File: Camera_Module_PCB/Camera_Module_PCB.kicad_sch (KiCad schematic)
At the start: 80 parts, among them J3 FFC2A32-24-T, SW2 SW_Push, SW3 SW_Push, U2 ESP32-S3R8, U4 MAX98357AETE_T, U5 AP3032KTR-G1, Y1 Q40,0-JXS10-8-10/10-FU-LF1

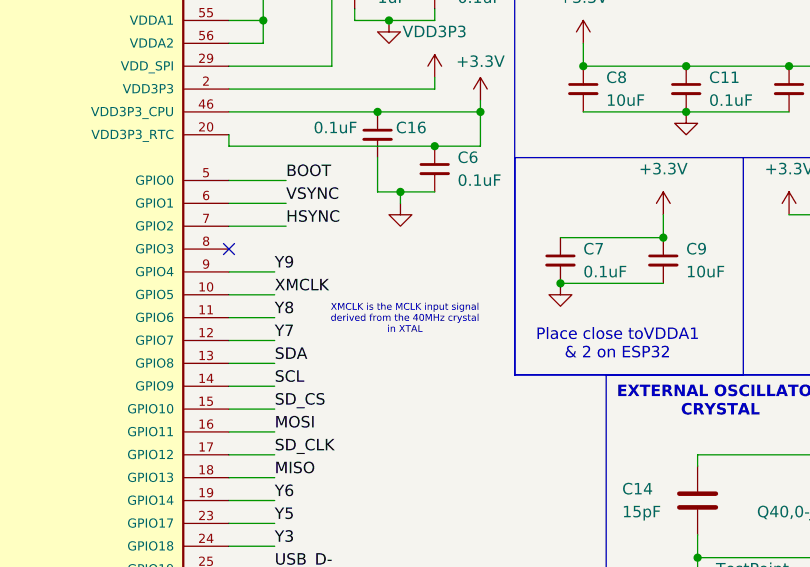
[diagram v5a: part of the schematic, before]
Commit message: Made some schematic edits & continued work on layout
Made some minor adjustments for the schematic to prepare for review. The layout continues to be built.
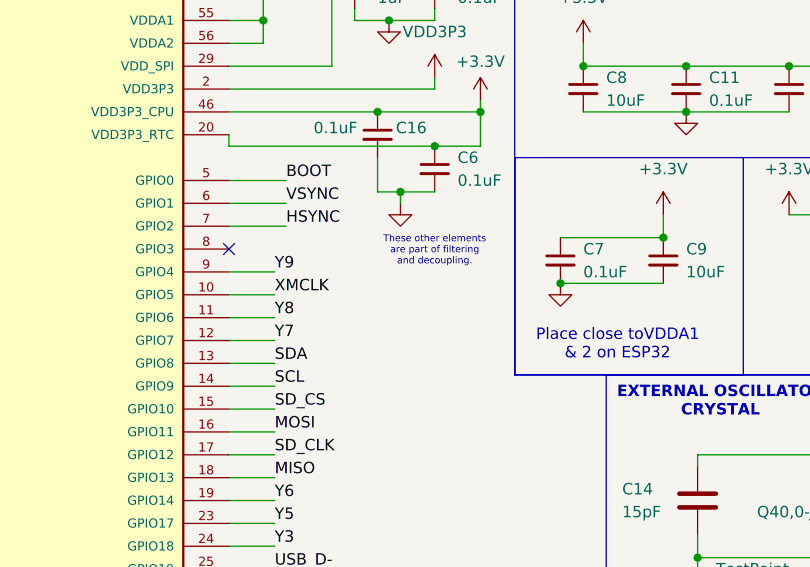
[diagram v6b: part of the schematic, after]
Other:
- note added: "These other elements are part of filtering and decoupling."
- note removed: "XMCLK is the MCLK input signal derived from the 40MHz crystal in XTAL"
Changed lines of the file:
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@@
 		(stroke
 			(width 0)
-			(type default)
+			(type solid)
+			(color 255 0 0 1)
 		)
 		(fill
@@
 		(stroke
 			(width 0)
-			(type default)
+			(type solid)
+			(color 250 0 0 1)
 		)
 		(fill
@@
 		(stroke
 			(width 0)
-			(type default)
+			(type solid)
+			(color 250 0 0 1)
 		)
 		(fill
@@
 		(stroke
 			(width 0)
-			(type default)
+			(type solid)
+			(color 251 0 0 1)
 		)
 		(fill
@@
 		)
 	)
-	(text "XMCLK is the MCLK input signal\nderived from the 40MHz crystal\nin XTAL"
+	(text "These other elements \nare part of filtering\nand decoupling.\n"
 		(exclude_from_sim no)
-		(at 320.548 59.944 0)
+		(at 323.85 52.324 0)
 		(effects
 			(font
 				(size 0.762 0.762)
+				(color 255 0 0 1)
 			)
 		)

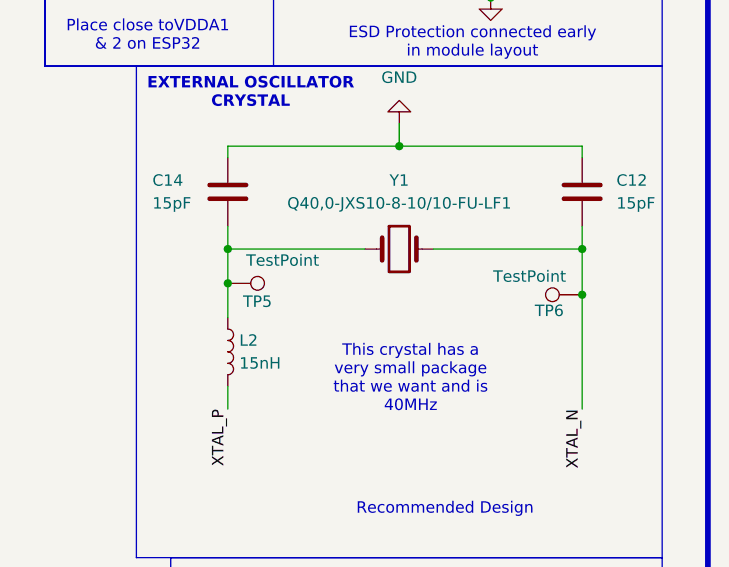
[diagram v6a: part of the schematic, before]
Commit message: Routed Antenna and Crystal
The antenna and crystals that connect to the ESP32-S3 were routed and a dense layer of ground vias were used for isolation along with no net filled zones. There is a small concern between the RF trace and the 3V3 analog power at pins 2 and 3. Due to DRC, I am unable to place vias between then. Perhaps much smaller vias can be used as a compromise.
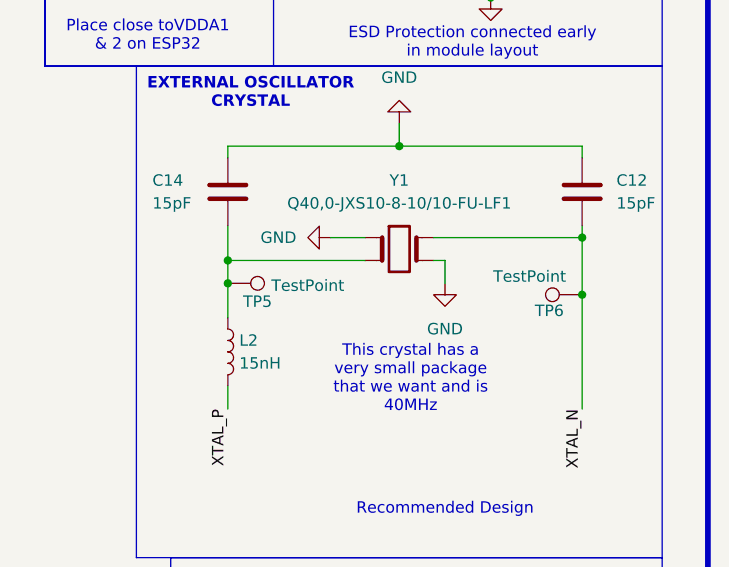
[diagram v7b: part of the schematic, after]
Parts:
- C7, C9: footprint Capacitor_SMD:C_0603_1608Metric -> Capacitor_SMD:C_0402_1005Metric
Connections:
- net GND: now also Y1.2 (Ground), Y1.4 (Ground)
- net XTAL_N: now also Y1.3 (Output); no longer Y1.2
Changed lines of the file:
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@@
 	)
 	(junction
+		(at 392.43 85.09)
+		(diameter 0)
+		(color 0 0 0 0)
+	)
+	(junction
 		(at 26.67 31.75)
 		(diameter 0)
@@
 	)
 	(junction
-		(at 392.43 86.36)
-		(diameter 0)
-		(color 0 0 0 0)
-	)
-	(junction
 		(at 114.3 45.72)
 		(diameter 0)
@@
 	)
 	(junction
+		(at 353.06 87.63)
+		(diameter 0)
+		(color 0 0 0 0)
+	)
+	(junction
 		(at 46.99 105.41)
 		(diameter 0)
@@
 	)
 	(junction
-		(at 353.06 86.36)
-		(diameter 0)
-		(color 0 0 0 0)
-	)
-	(junction
 		(at 198.12 74.93)
 		(diameter 0)
@@
 	(wire
 		(pts
-			(xy 353.06 86.36) (xy 353.06 90.17)
-		)
-		(stroke
-			(width 0)
-			(type default)
-		)
-	)
-	(wire
-		(pts
 			(xy 363.22 31.75) (xy 369.57 31.75)
 		)
@@
 	(wire
 		(pts
-			(xy 392.43 86.36) (xy 392.43 83.82)
-		)
-		(stroke
-			(width 0)
-			(type default)
-		)
-	)
-	(wire
-		(pts
 			(xy 20.32 105.41) (xy 21.59 105.41)
 		)
@@
 	(wire
 		(pts
-			(xy 353.06 83.82) (xy 353.06 86.36)
+			(xy 353.06 83.82) (xy 353.06 87.63)
 		)
 		(stroke
@@
 	(wire
 		(pts
+			(xy 377.19 87.63) (xy 377.19 90.17)
+		)
+		(stroke
+			(width 0)
+			(type default)
+		)
+	)
+	(wire
+		(pts
 			(xy 300.99 107.95) (xy 306.07 107.95)
 		)
@@
 	(wire
 		(pts
+			(xy 364.49 85.09) (xy 368.3 85.09)
+		)
+		(stroke
+			(width 0)
+			(type default)
+		)
+	)
+	(wire
+		(pts
 			(xy 382.27 137.16) (xy 382.27 149.86)
 		)
@@
 	(wire
 		(pts
-			(xy 375.92 86.36) (xy 392.43 86.36)
+			(xy 375.92 85.09) (xy 392.43 85.09)
 		)
 		(stroke
@@
 	(wire
 		(pts
+			(xy 392.43 85.09) (xy 392.43 83.82)
+		)
+		(stroke
+			(width 0)
+			(type default)
+		)
+	)
+	(wire
+		(pts
 			(xy 106.68 43.18) (xy 95.25 43.18)
 		)
@@
 	(wire
 		(pts
-			(xy 353.06 86.36) (xy 368.3 86.36)
+			(xy 353.06 87.63) (xy 368.3 87.63)
 		)
 		(stroke
@@
 	(wire
 		(pts
+			(xy 353.06 87.63) (xy 353.06 90.17)
+		)
+		(stroke
+			(width 0)
+			(type default)
+		)
+	)
+	(wire
+		(pts
 			(xy 262.89 204.47) (xy 251.46 204.47)
 		)
@@
 	(wire
 		(pts
+			(xy 392.43 85.09) (xy 392.43 91.44)
+		)
+		(stroke
+			(width 0)
+			(type default)
+		)
+	)
+	(wire
+		(pts
 			(xy 262.89 196.85) (xy 262.89 199.39)
 		)
@@
 	(wire
 		(pts
-			(xy 242.57 87.63) (xy 248.92 87.63)
+			(xy 375.92 87.63) (xy 377.19 87.63)
 		)
 		(stroke
@@
 	(wire
 		(pts
-			(xy 392.43 91.44) (xy 392.43 104.14)
+			(xy 242.57 87.63) (xy 248.92 87.63)
 		)
 		(stroke
@@
 	(wire
 		(pts
-			(xy 26.67 162.56) (xy 29.21 162.56)
+			(xy 392.43 91.44) (xy 392.43 104.14)
 		)
 		(stroke
@@
 	(wire
 		(pts
-			(xy 33.02 227.33) (xy 33.02 228.6)
+			(xy 26.67 162.56) (xy 29.21 162.56)
 		)
 		(stroke
@@
 	(wire
 		(pts
-			(xy 20.32 105.41) (xy 20.32 102.87)
+			(xy 33.02 227.33) (xy 33.02 228.6)
 		)
 		(stroke
@@
 	(wire
 		(pts
-			(xy 83.82 93.98) (xy 82.55 93.98)
+			(xy 20.32 105.41) (xy 20.32 102.87)
 		)
 		(stroke
@@
 	(wire
 		(pts
-			(xy 240.03 102.87) (xy 240.03 99.06)
+			(xy 83.82 93.98) (xy 82.55 93.98)
 		)
 		(stroke
@@
 	(wire
 		(pts
-			(xy 392.43 86.36) (xy 392.43 91.44)
+			(xy 240.03 102.87) (xy 240.03 99.06)
 		)
 		(stroke
@@
 	)
 	(symbol
+		(lib_id "power:GND")
+		(at 377.19 90.17 0)
+		(unit 1)
+		(exclude_from_sim no)
+		(in_bom yes)
+		(on_board yes)
+		(dnp no)
+		(fields_autoplaced yes)
+		(property "Reference" "#PWR066"
+			(at 377.19 96.52 0)
+			(effects
+				(font
+					(size 1.27 1.27)
+				)
+				(hide yes)
+			)
+		)
+		(property "Value" "GND"
+			(at 377.19 95.25 0)
+			(effects
+				(font
+					(size 1.27 1.27)
+				)
+			)
+		)
+		(property "Footprint" ""
+			(at 377.19 90.17 0)
+			(effects
+				(font
+					(size 1.27 1.27)
+				)
+				(hide yes)
+			)
+		)
+		(property "Datasheet" ""
+			(at 377.19 90.17 0)
+			(effects
+				(font
+					(size 1.27 1.27)
+				)
+				(hide yes)
+			)
+		)
+		(property "Description" "Power symbol creates a global label with name \"GND\" , ground"
+			(at 377.19 90.17 0)
+			(effects
+				(font
+					(size 1.27 1.27)
+				)
+				(hide yes)
+			)
+		)
+		(pin "1"
+		)
+		(instances
+			(project ""
+				(path "/e3d5a9d6-7dc8-43b3-bd64-189ae9cbab33"
+					(reference "#PWR066")
+					(unit 1)
+				)
+			)
+		)
+	)
+	(symbol
 		(lib_id "Connector:TestPoint")
 		(at 353.06 90.17 270)
@@
 		)
 		(property "Value" "TestPoint"
-			(at 359.156 87.63 90)
+			(at 361.95 90.424 90)
 			(effects
 				(font
@@
 			)
 		)
-		(property "Footprint" "Capacitor_SMD:C_0603_1608Metric"
+		(property "Footprint" "Capacitor_SMD:C_0402_1005Metric"
 			(at 349.25 53.34 0)
 			(effects
@@
 			)
 		)
-		(property "Footprint" "Capacitor_SMD:C_0603_1608Metric"
+		(property "Footprint" "Capacitor_SMD:C_0402_1005Metric"
 			(at 337.82 53.34 0)
 			(effects
@@
 	)
 	(symbol
+		(lib_id "power:GND")
+		(at 364.49 85.09 270)
+		(unit 1)
+		(exclude_from_sim no)
+		(in_bom yes)
+		(on_board yes)
+		(dnp no)
+		(fields_autoplaced yes)
+		(property "Reference" "#PWR067"
+			(at 358.14 85.09 0)
+			(effects
+				(font
+					(size 1.27 1.27)
+				)
+				(hide yes)
+			)
+		)
+		(property "Value" "GND"
+			(at 360.68 85.0899 90)
+			(effects
+				(font
+					(size 1.27 1.27)
+				)
+				(justify right)
+			)
+		)
+		(property "Footprint" ""
+			(at 364.49 85.09 0)
+			(effects
+				(font
+					(size 1.27 1.27)
+				)
+				(hide yes)
+			)
+		)
+		(property "Datasheet" ""
+			(at 364.49 85.09 0)
+			(effects
+				(font
+					(size 1.27 1.27)
+				)
+				(hide yes)
+			)
+		)
+		(property "Description" "Power symbol creates a global label with name \"GND\" , ground"
+			(at 364.49 85.09 0)
+			(effects
+				(font
+					(size 1.27 1.27)
+				)
+				(hide yes)
+			)
+		)
+		(pin "1"
+		)
+		(instances
+			(project "Camera_Module_PCB"
+				(path "/e3d5a9d6-7dc8-43b3-bd64-189ae9cbab33"
+					(reference "#PWR067")
+					(unit 1)
+				)
+			)
+		)
+	)
+	(symbol
 		(lib_id "Device:C_Small")
 		(at 317.5 39.37 0)
@@
 		(pin "2"
 		)
+		(pin "3"
+		)
+		(pin "4"
+		)
 		(instances

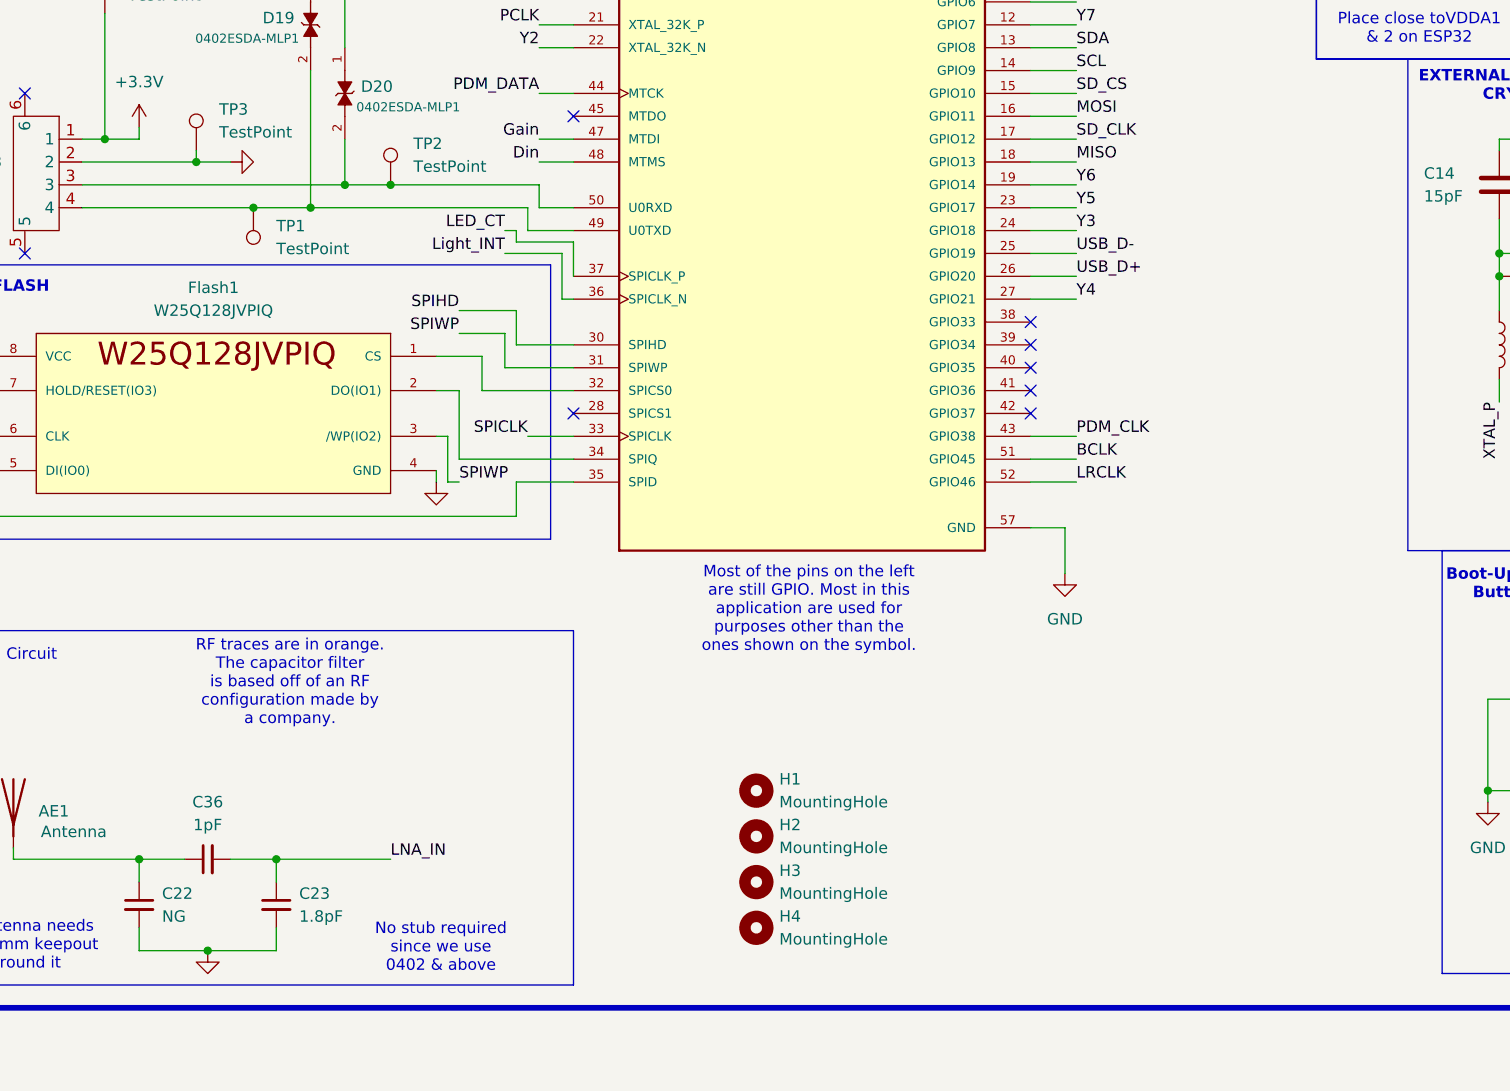
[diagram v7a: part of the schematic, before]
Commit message: Continued Routing of ESP32 chip and USB
Continued to create general layouts for the necessary ESP32 chip and power suuply
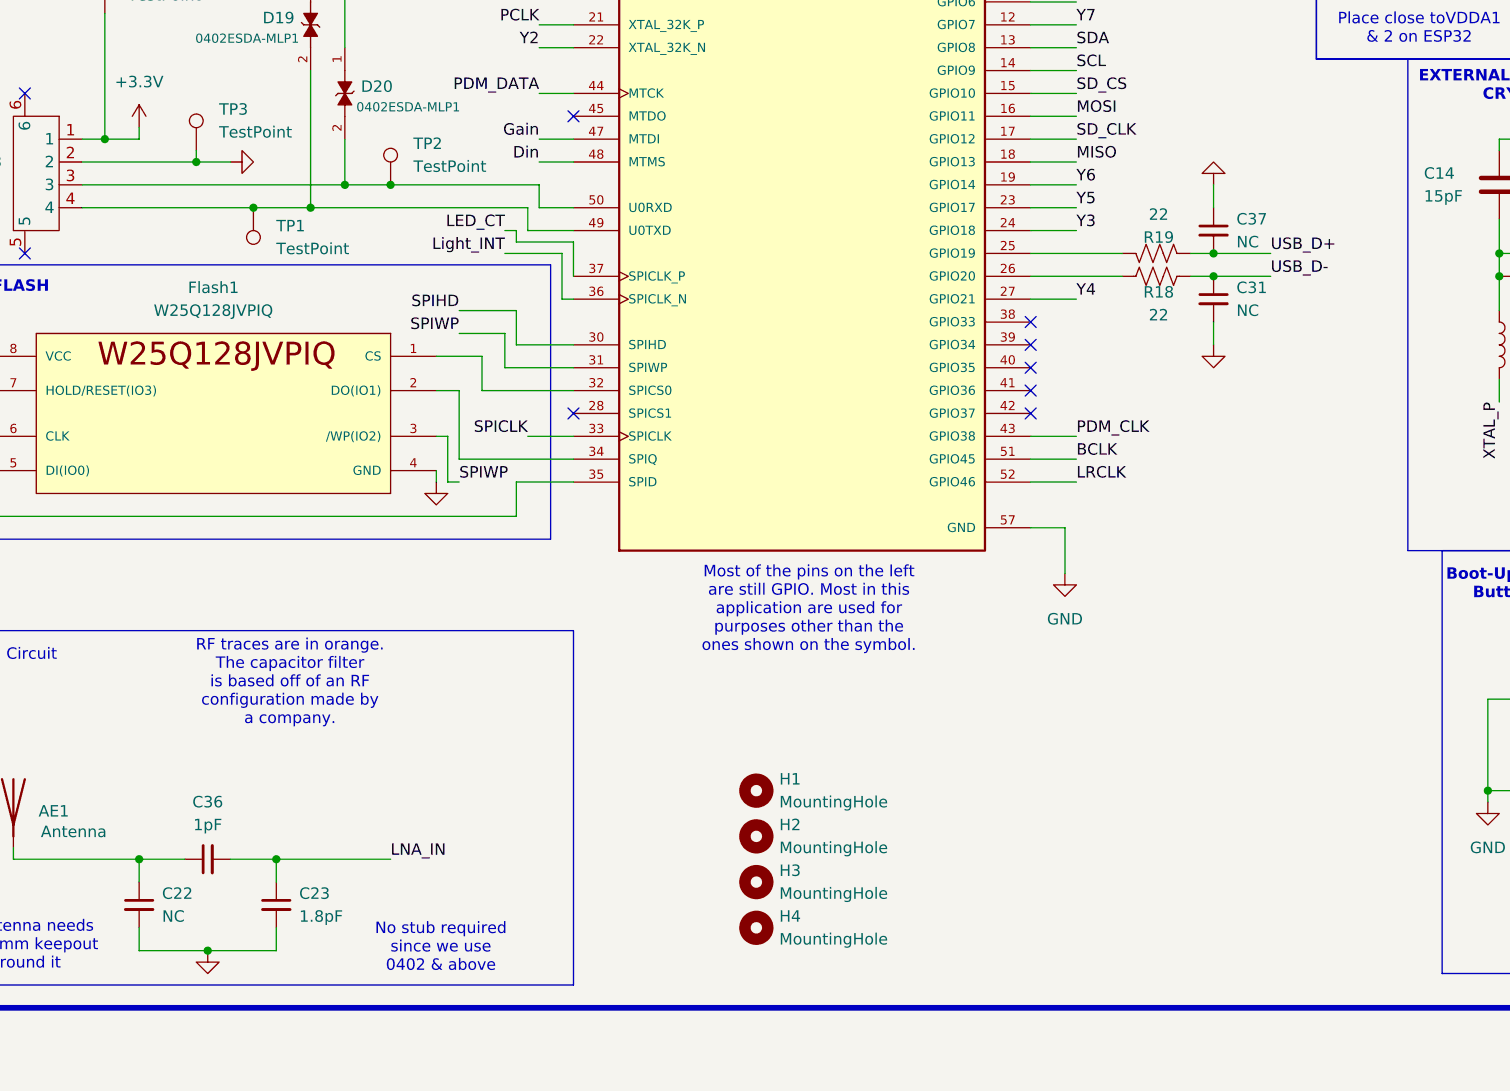
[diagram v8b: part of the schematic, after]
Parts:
- added C31, C37: NC, Capacitor_SMD:C_0402_1005Metric, symbol Device:C_Small
- added R18, R19: 22, Resistor_SMD:R_0402_1005Metric, symbol Device:R_US
- C22: value NG -> NC
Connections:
- net GND: now also C31.2, C37.1
- net USB_D+: now also C37.2, R19.2; no longer U2.26 (GPIO20)
- net USB_D-: now also C31.1, R18.2; no longer U2.25 (GPIO19)
- new net: R19.1, U2.25 (GPIO19)
- new net: R18.1, U2.26 (GPIO20)
